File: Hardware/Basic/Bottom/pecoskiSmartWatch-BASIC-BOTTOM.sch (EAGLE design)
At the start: 31 parts, among them U1 AD5242-SO16

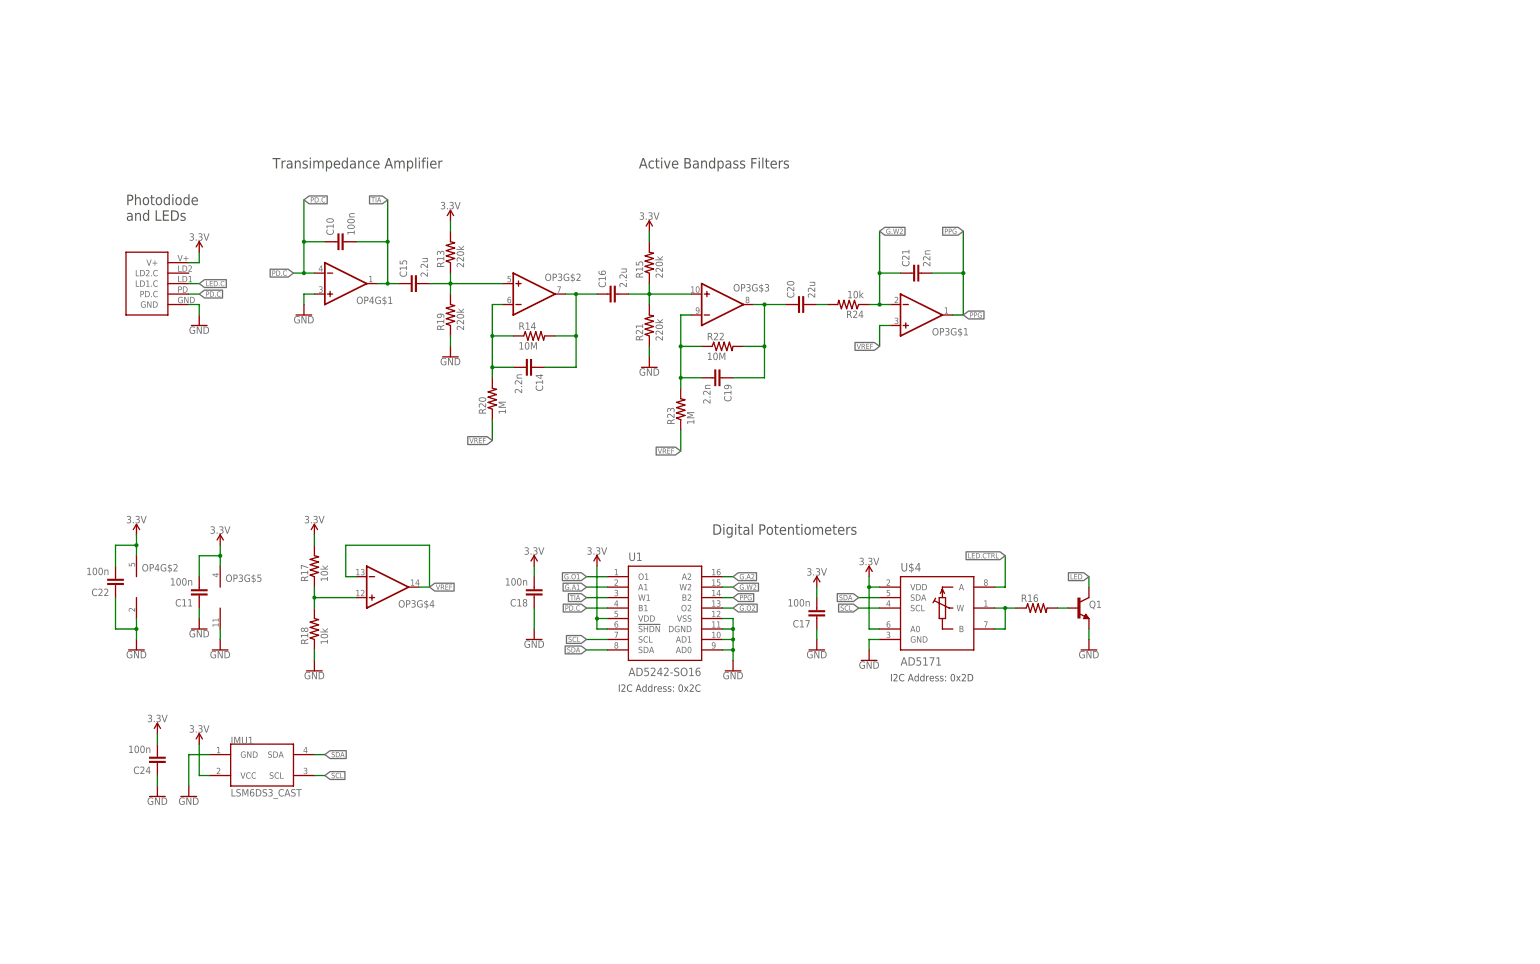
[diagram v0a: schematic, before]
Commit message: Updated Eagle Hardware 2021_02_27
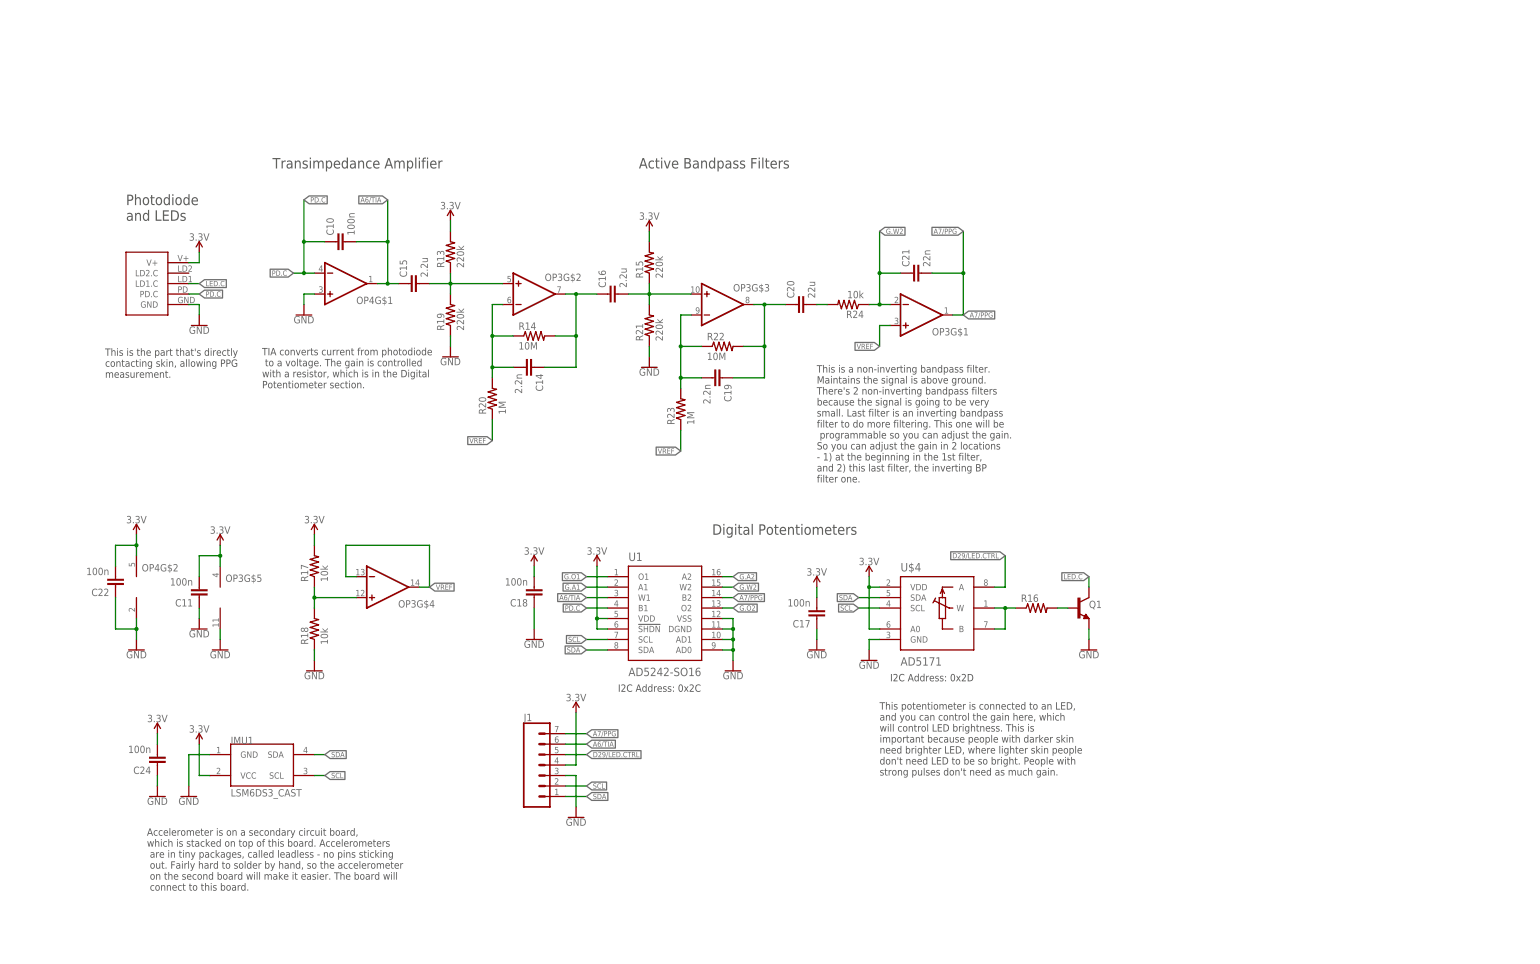
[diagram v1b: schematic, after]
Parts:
- added J1: (no value), LinnesLab-Connectors:CONN_07-1.27MM
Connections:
- removed net LED: Q1.C
- removed net LED.CTRL: U$4.A
- removed net PPG: C21.2, OP3G$1.OUT, U1.B2
- removed net TIA: C10.2, C15.1, OP4G$1.OUT, U1.W1
- new net A6/TIA: C10.2, C15.1, J1.6, OP4G$1.OUT, U1.W1
- new net A7/PPG: C21.2, J1.7, OP3G$1.OUT, U1.B2
- new net D29/LED.CTRL: J1.5, U$4.A
- net 3.3V: now also J1.4
- net GND: now also J1.3
- net LED.C: now also Q1.C
- net SCL: now also J1.2
- net SDA: now also J1.1
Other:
- note added: "Accelerometer is on a secondary circuit board, which is stacked on top of this board. Accelerometers are in tiny packages, called leadless - no pins sticking out. Fairly hard to solder by hand, so the accelerometer on the second board will make it easier. The board will connect to this board."
- note added: "TIA converts current from photodiode to a voltage. The gain is controlled with a resistor, which is in the Digital Potentiometer section."
- note added: "This is a non-inverting bandpass filter. Maintains the signal is above ground. There's 2 non-inverting bandpass filters because the signal is going to be very small. Last filter is an inverting bandpass filter to do more filtering. This one will be programmable so you can adjust the gain. So you can adjust the gain in 2 locations - 1) at the beginning in the 1st filter, and 2) this last filter, t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"
- note added: "This is the part that's directly contacting skin, allowing PPG measurement."
- note added: "This potentiometer is connected to an LED, and you can control the gain here, which will control LED brightness. This is important because people with darker skin need brighter LED, where lighter skin people don't need LED to be so bright. People with strong pulses don't need as much gain."
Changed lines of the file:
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@@
 <part name="GND30" library="LinnesLab-Symbols" deviceset="GND" device=""/>
 <part name="SUPPLY24" library="LinnesLab-Symbols" deviceset="3.3V" device=""/>
+<part name="J1" library="LinnesLab-Connectors" deviceset="CONN_07" device="-1.27MM"/>
+<part name="GND1" library="LinnesLab-Symbols" deviceset="GND" device=""/>
+<part name="SUPPLY1" library="LinnesLab-Symbols" deviceset="3.3V" device=""/>
 </parts>
 <sheets>
@@
 <text x="134.62" y="-2.54" size="1.778" layer="97" ratio="15">I2C Address: 0x2C</text>
 <text x="200.66" y="0" size="1.778" layer="97" ratio="15">I2C Address: 0x2D</text>
+<text x="10.16" y="73.66" size="1.778" layer="97">This is the part that's directly
+contacting skin, allowing PPG
+measurement.</text>
+<text x="48.26" y="71.12" size="1.778" layer="97">TIA converts current from photodiode
+ to a voltage. The gain is controlled
+with a resistor, which is in the Digital
+Potentiometer section. </text>
+<text x="182.88" y="48.26" size="1.778" layer="97">This is a non-inverting bandpass filter.
+Maintains the signal is above ground.
+There's 2 non-inverting bandpass filters
+because the signal is going to be very
+small. Last filter is an inverting bandpass
+filter to do more filtering. This one will be
+ programmable so you can adjust the gain.
+So you can adjust the gain in 2 locations
+- 1) at the beginning in the 1st filter,
+and 2) this last filter, the inverting BP
+filter one.</text>
+<text x="198.12" y="-22.86" size="1.778" layer="97">This potentiometer is connected to an LED,
+and you can control the gain here, which
+will control LED brightness. This is
+important because people with darker skin
+need brighter LED, where lighter skin people
+don't need LED to be so bright. People with
+strong pulses don't need as much gain.</text>
+<text x="20.32" y="-50.8" size="1.778" layer="97">Accelerometer is on a secondary circuit board,
+which is stacked on top of this board. Accelerometers
+ are in tiny packages, called leadless - no pins sticking
+ out. Fairly hard to solder by hand, so the accelerometer
+ on the second board will make it easier. The board will
+ connect to this board.</text>
 </plain>
 <instances>
@@
 <instance part="SUPPLY24" gate="G$1" x="22.86" y="-12.7" smashed="yes">
 <attribute name="VALUE" x="22.86" y="-9.906" size="1.778" layer="96" align="bottom-center"/>
+</instance>
+<instance part="J1" gate="G$1" x="116.84" y="-22.86" smashed="yes">
+<attribute name="VALUE" x="111.76" y="-32.766" size="1.778" layer="96" font="vector"/>
+<attribute name="NAME" x="111.76" y="-9.652" size="1.778" layer="95" font="vector"/>
+</instance>
+<instance part="GND1" gate="G$1" x="124.46" y="-33.02" smashed="yes">
+<attribute name="VALUE" x="124.46" y="-33.274" size="1.778" layer="96" align="top-center"/>
+</instance>
+<instance part="SUPPLY1" gate="G$1" x="124.46" y="-7.62" smashed="yes">
+<attribute name="VALUE" x="124.46" y="-4.826" size="1.778" layer="96" align="bottom-center"/>
 </instance>
 </instances>
@@
 <wire x1="22.86" y1="-25.4" x2="22.86" y2="-22.86" width="0.1524" layer="91"/>
 </segment>
+<segment>
+<pinref part="J1" gate="G$1" pin="3"/>
+<wire x1="121.92" y1="-22.86" x2="124.46" y2="-22.86" width="0.1524" layer="91"/>
+<pinref part="GND1" gate="G$1" pin="GND"/>
+<wire x1="124.46" y1="-22.86" x2="124.46" y2="-30.48" width="0.1524" layer="91"/>
+</segment>
 </net>
 <net name="3.3V" class="0">
@@
 <wire x1="22.86" y1="-12.7" x2="22.86" y2="-15.24" width="0.1524" layer="91"/>
 </segment>
+<segment>
+<pinref part="J1" gate="G$1" pin="4"/>
+<wire x1="121.92" y1="-20.32" x2="124.46" y2="-20.32" width="0.1524" layer="91"/>
+<pinref part="SUPPLY1" gate="G$1" pin="3.3V"/>
+<wire x1="124.46" y1="-20.32" x2="124.46" y2="-7.62" width="0.1524" layer="91"/>
+</segment>
 </net>
 <net name="SDA" class="0">
@@
 <label x="63.5" y="-17.78" size="1.27" layer="95" xref="yes"/>
 </segment>
+<segment>
+<pinref part="J1" gate="G$1" pin="1"/>
+<wire x1="121.92" y1="-27.94" x2="127" y2="-27.94" width="0.1524" layer="91"/>
+<label x="127" y="-27.94" size="1.27" layer="95" xref="yes"/>
+</segment>
 </net>
 <net name="SCL" class="0">
@@
 <label x="63.5" y="-22.86" size="1.27" layer="95" xref="yes"/>
 </segment>
-</net>
-<net name="TIA" class="0">
+<segment>
+<pinref part="J1" gate="G$1" pin="2"/>
+<wire x1="121.92" y1="-25.4" x2="127" y2="-25.4" width="0.1524" layer="91"/>
+<label x="127" y="-25.4" size="1.27" layer="95" xref="yes"/>
+</segment>
+</net>
+<net name="A6/TIA" class="0">
 <segment>
 <wire x1="132.08" y1="20.32" x2="127" y2="20.32" width="0.1524" layer="91"/>
@@
 <junction x="78.74" y="96.52"/>
 </segment>
+<segment>
+<pinref part="J1" gate="G$1" pin="6"/>
+<wire x1="121.92" y1="-15.24" x2="127" y2="-15.24" width="0.1524" layer="91"/>
+<label x="127" y="-15.24" size="1.27" layer="95" xref="yes"/>
+</segment>
 </net>
 <net name="PD.C" class="0">
@@
 <label x="33.02" y="96.52" size="1.27" layer="95" xref="yes"/>
 </segment>
+<segment>
+<wire x1="248.92" y1="22.86" x2="248.92" y2="25.4" width="0.1524" layer="91"/>
+<label x="248.92" y="25.4" size="1.27" layer="95" rot="R180" xref="yes"/>
+<pinref part="Q1" gate="G$1" pin="C"/>
+</segment>
 </net>
 <net name="VREF" class="0">
@@
 <wire x1="198.12" y1="86.36" x2="198.12" y2="81.28" width="0.1524" layer="91"/>
 <label x="198.12" y="81.28" size="1.27" layer="95" rot="R180" xref="yes"/>
-</segment>
-</net>
-<net name="LED" class="0">
-<segment>
-<wire x1="248.92" y1="22.86" x2="248.92" y2="25.4" width="0.1524" layer="91"/>
-<label x="248.92" y="25.4" size="1.27" layer="95" rot="R180" xref="yes"/>
-<pinref part="Q1" gate="G$1" pin="C"/>
 </segment>
 </net>
@@
 </segment>
 </net>
-<net name="LED.CTRL" class="0">
+<net name="D29/LED.CTRL" class="0">
 <segment>
 <pinref part="U$4" gate="G$1" pin="A"/>
@@
 <wire x1="228.6" y1="22.86" x2="228.6" y2="30.48" width="0.1524" layer="91"/>
 <label x="228.6" y="30.48" size="1.27" layer="95" rot="R180" xref="yes"/>
+</segment>
+<segment>
+<pinref part="J1" gate="G$1" pin="5"/>
+<wire x1="121.92" y1="-17.78" x2="127" y2="-17.78" width="0.1524" layer="91"/>
+<label x="127" y="-17.78" size="1.27" layer="95" xref="yes"/>
 </segment>
 </net>
@@
 </segment>
 </net>
-<net name="PPG" class="0">
+<net name="A7/PPG" class="0">
 <segment>
 <wire x1="160.02" y1="20.32" x2="162.56" y2="20.32" width="0.1524" layer="91"/>
@@
 <label x="218.44" y="88.9" size="1.27" layer="95" xref="yes"/>
 </segment>
-</net>
+<segment>
+<pinref part="J1" gate="G$1" pin="7"/>
+<wire x1="121.92" y1="-12.7" x2="127" y2="-12.7" width="0.1524" layer="91"/>
+<label x="127" y="-12.7" size="1.27" layer="95" xref="yes"/>
+</segment>
+</net>

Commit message: Hardware Updates 2021_02_27
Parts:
- renumbered OP4 to TIA, U$4 to AD517, U1 to AD5242

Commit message: HW Updates 2021/03/06
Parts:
- added C1: 100n, LinnesLab-Passives:CAPACITOR0603
- added LOGO1: REVISION.A, LinnesLab-Logos:REVISION.A
- added LOGO2: OSHW-LOGOS, LinnesLab-Logos:OSHW-LOGOS
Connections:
- net GND: now also C1.2
- net VREF: now also C1.1
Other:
- note added: "Castellated IMU breakout"
- note added: "Connection to digital potentiometer for dynamic gain control."
- note added: "Connection to optimal sensing module."
- note added: "Connection to upper board."
- note added: "Pecoski SmartWatch PPG Circuit"
- note added: "Vref Generator and Bypass Capacitor"
- moved on the sheet: C11, C22, J1, OP3G$4, OP3G$5, R17, R18, TIAG$2

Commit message: Updated HW 2021_03_13 AM
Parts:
- added C2: 1u, LinnesLab-Passives:CAPACITOR0603
- added U2: PCF8523, LinnesLab-Clocks:PCF8523
- added Y2: 32.7680kHz, LinnesLab-Clocks:CRYSTALECS-.327-12.5-12-C-TR
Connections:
- new net N$1: U2.OSCO, Y2.1
- new net N$2: U2.OSCI, Y2.2
- net 3.3V: now also C2.1, U2.VDD
- net GND: now also C2.2, U2.VSS
- net SCL: now also U2.SCL
- net SDA: now also U2.SDA
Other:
- note added: "Back-up battery if desired"
- note added: "I2C Address = 0x68h"
- note added: "Real-Time Clock"

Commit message: Updated HW 2021_03_13 PM
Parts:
- added C3, C4: 4.7u, LinnesLab-Passives:CAPACITOR0603
- added C6, C9: 1u, LinnesLab-Passives:CAPACITOR0603
- added CHRG: MCP73831, LinnesLab-Power:MCP73831
- added LDO1: MIC5504, LinnesLab-Power:MIC5504
- added R3: 100k, LinnesLab-Passives:RESISTOR0603
- added R4: (no value), LinnesLab-Passives:RESISTOR0603
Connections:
- new net D27/CHRG.STATUS: CHRG.STAT, R3.1
- new net N$3: CHRG.PROG, R4.2
- new net VIN1: C4.2, C6.2, CHRG.VIN, LDO1.EN, LDO1.IN, R3.2
- new net VLIPO: C3.1, CHRG.VBAT
- net 3.3V: now also C9.1, LDO1.OUT
- net GND: now also C3.2, C4.1, C6.1, C9.2, CHRG.VSS, LDO1.GND, R4.1
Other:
- note added: "Digital Output"
